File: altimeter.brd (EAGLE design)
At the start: 27.5 x 15 mm, 22 parts, among them U1 DPS310, U2 WT51822-S4ATMODULE, U3 MMA8452Q, U4 MIC5205-3.3YM5-TR

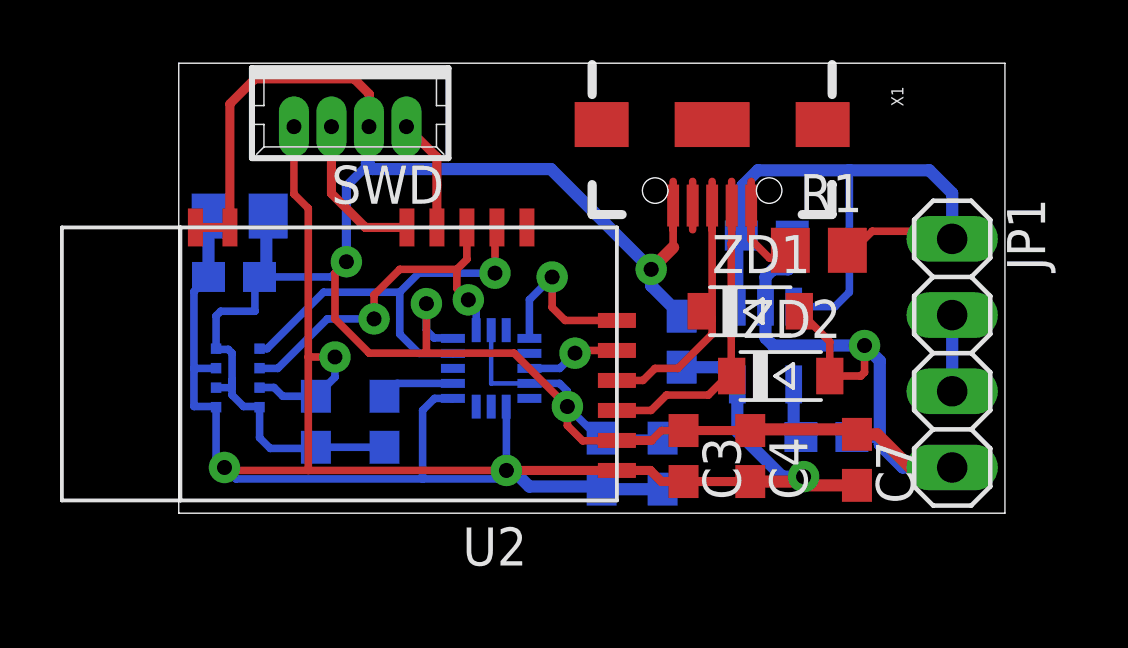
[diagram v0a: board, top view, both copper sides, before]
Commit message: Silkscreen cleanup before gerber export.
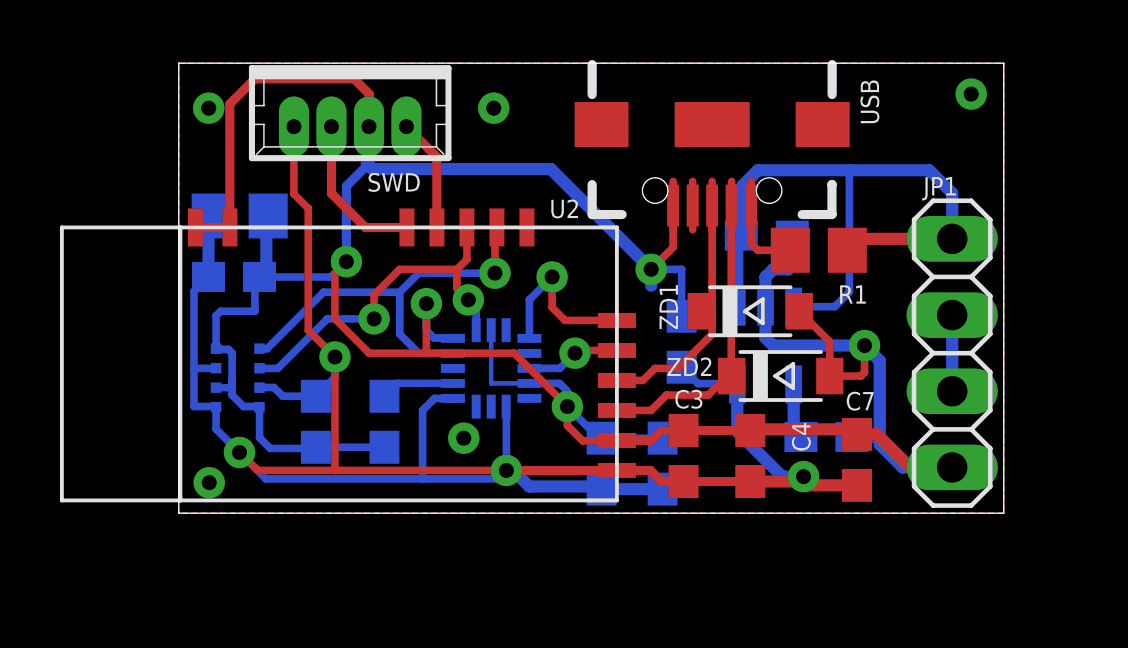
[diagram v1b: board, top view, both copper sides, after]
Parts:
- renumbered X1 to USB
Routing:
- net +3V3: track 75.2 -> 73.8 mm
- net GND: track 108.0 -> 109.1 mm, vias 5 -> 10
- added copper zone on layer 1, net GND
- added copper zone on layer 16, net GND
